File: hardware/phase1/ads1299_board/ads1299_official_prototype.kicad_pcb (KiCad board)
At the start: 4 copper layers, 117 parts, among them J3 Conn_02x10_Odd_Even, J6 36PIN_IDC, U1 ADS1299IPAG, U10 24AA256-I/ST, U4 OPA376

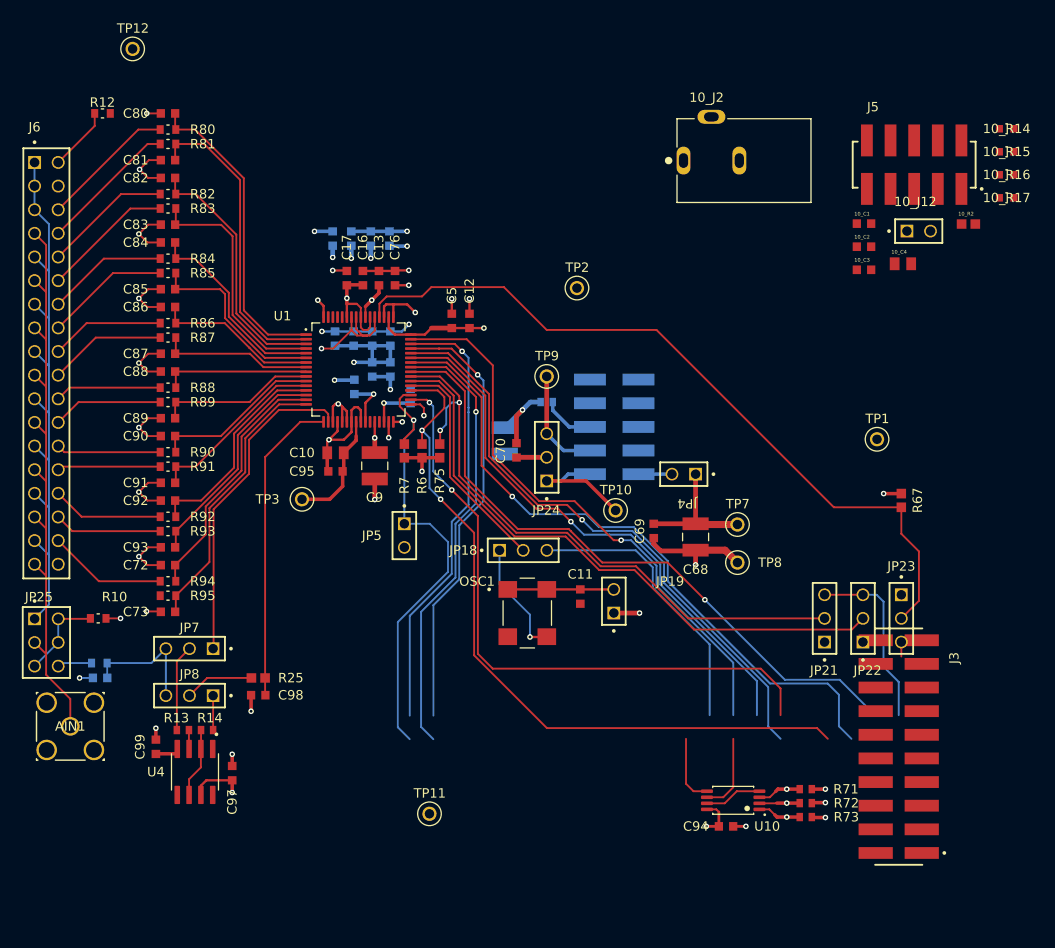
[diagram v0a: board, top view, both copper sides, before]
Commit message: ADS1299 Updated J3 and organized routes, speeding up placement and routing
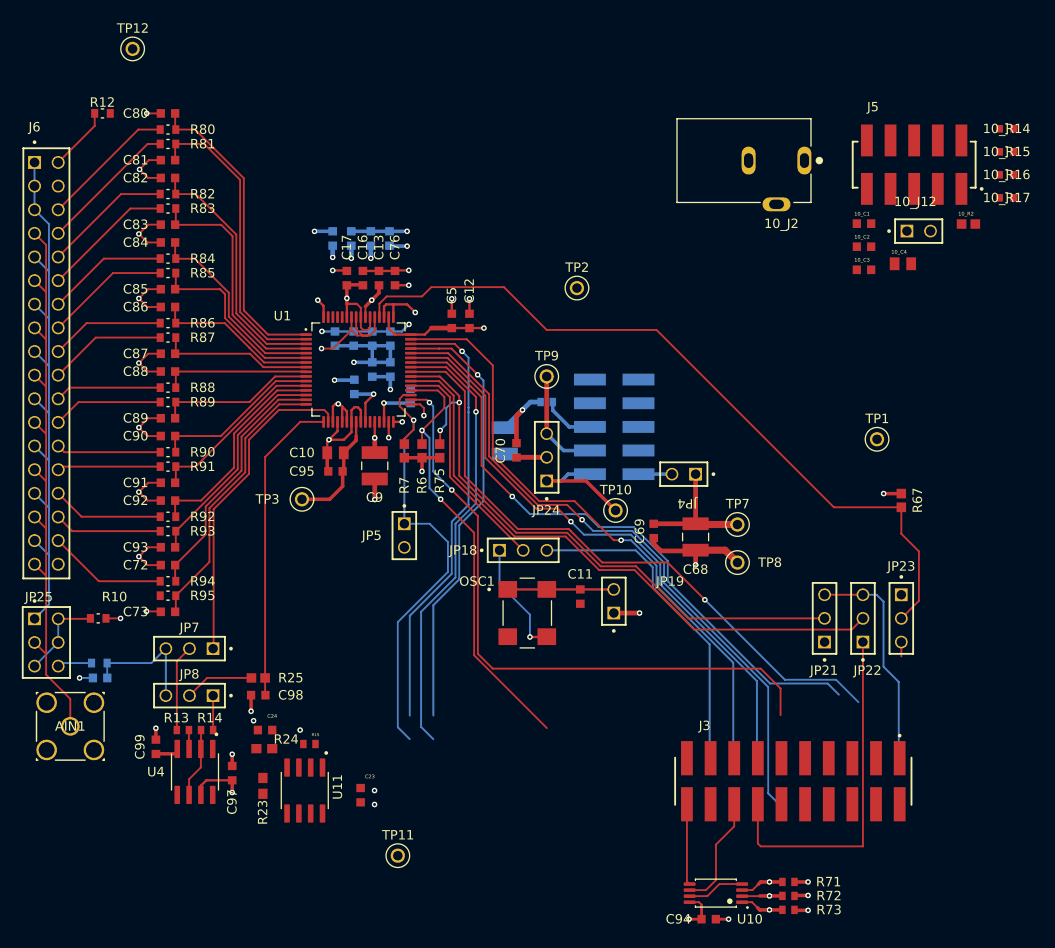
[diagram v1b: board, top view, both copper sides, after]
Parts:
- added C23: CAPC1608X90N, GRM188R61E105KA12D:CAPC1608X90N, F.Cu at (127.0, 97.0)
- added C24: CAPC1608X90N, GRM188R61E105KA12D:CAPC1608X90N, F.Cu at (116.7, 90.0)
- added R15: RESC1005X40, RC0402JR-070RL:RESC1005X40, F.Cu at (121.5, 91.5)
- added R23: 0603, RC0603JR-072ML:0603, F.Cu at (116.5, 96.0)
- added R24: 0603, RC0603JR-072ML:0603, F.Cu at (116.7, 92.0)
- added U11: SOIC127P599X175-8N, OPA376AID:SOIC127P599X175-8N, F.Cu at (121.0, 96.5)
- moved J3 11.9 mm to (173.5, 95.5), turned to 0 degrees
- moved C94 10.1 mm to (164.4, 110.3)
- moved R71 10.1 mm to (173.0, 106.3)
- moved R72 10.1 mm to (173.0, 107.8)
- moved R73 10.1 mm to (173.0, 109.3)
- moved U10 10.1 mm to (165.2, 107.5)
- moved TP11 5.64 mm to (131.0, 103.5)
- turned 10_J2 to 180 degrees
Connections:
- J3 pad 03: (no net) -> CLK
- J3 pad 06: (no net) -> GPIO1
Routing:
- net Net-(J3-Pin_14): track 0.00 -> 37.7 mm
- net /RESET: track 78.2 -> 47.5 mm
- net GPIO2: track 64.6 -> 71.6 mm
- net GPIO1: track 71.7 -> 66.4 mm
- net SPI_DRDY: track 61.6 -> 66.2 mm
- net Net-(J3-Pin_1): track 19.5 -> 24.1 mm
- net EXT_CLK: track 30.6 -> 35.2 mm
- net SPI_OUT: track 60.4 -> 65.0 mm
- net /SCL: track 8.49 -> 12.2 mm
- net SPI_CLK: track 70.5 -> 68.2 mm
- net /SDA: track 7.41 -> 8.70 mm
- net GNDA: vias 26 -> 30

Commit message: Schematic changes, no more power stuff from external board. Layout work, added power stuff, lots to do
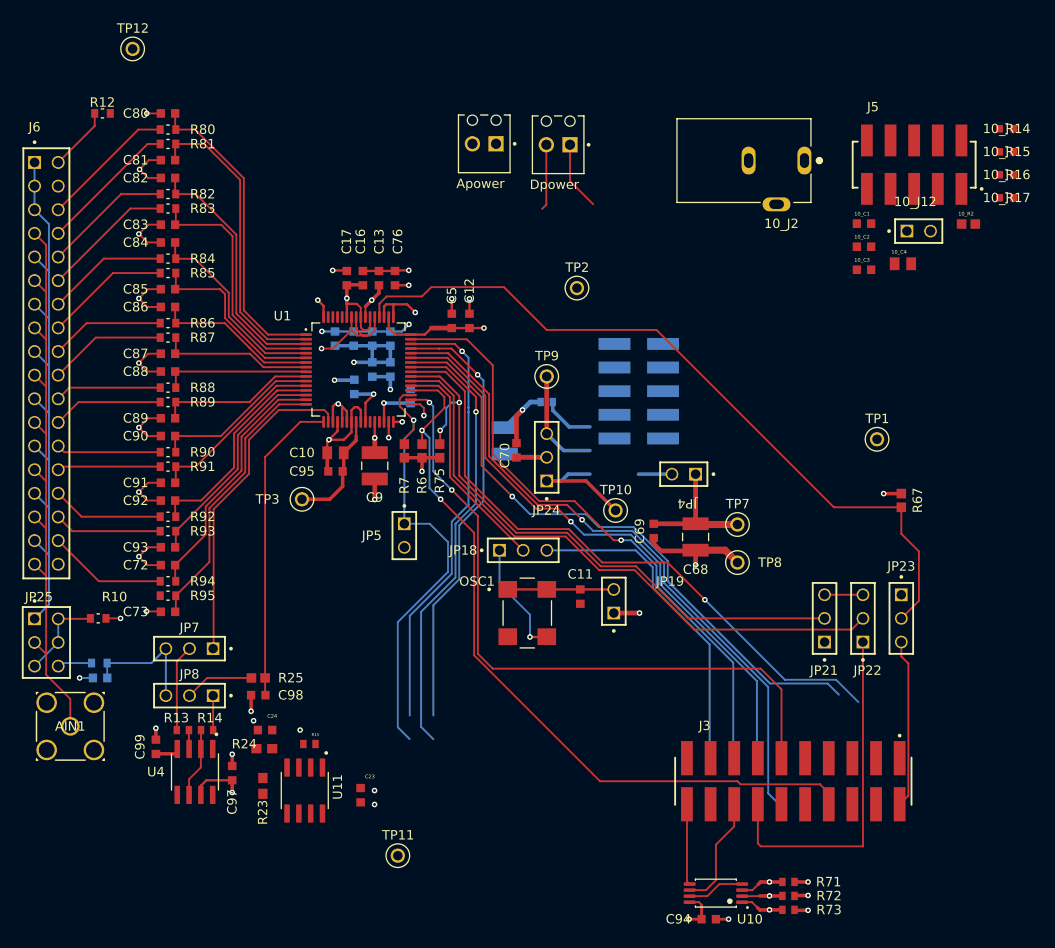
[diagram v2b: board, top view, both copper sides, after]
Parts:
- removed C3, C7, C77, C8: 1uF, GRM188R61E105KA12D:CAPC1608X90N
- added Apower: PHOENIX_1725656, 1725656:PHOENIX_1725656, F.Cu at (143.1, 23.9)
- added Dpower: PHOENIX_1725656, 1725656:PHOENIX_1725656, F.Cu at (151.0, 24.0)
- moved J4 4.66 mm to (156.9, 53.6)
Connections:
- J3 pad 01: (no net) -> GND
- J3 pad 02: (no net) -> Net-(J3-Pin_2)
- J3 pad 04: (no net) -> GNDA
- J3 pad 05: (no net) -> unconnected-(j3-Pin_5-Pad5)
- J3 pad 07: (no net) -> SPI_CS
- J3 pad 08: (no net) -> /RESET
- J3 pad 09: (no net) -> unconnected-(J3-Pin_9-Pad9)
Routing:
- net /RESET: track 47.5 -> 83.0 mm
- net Net-(J3-Pin_1): track 24.1 -> 4.12 mm
- net Net-(J3-Pin_2): track 1.55 -> 18.1 mm
- net GND: track 29.6 -> 37.1 mm
- net DVDD: track 29.9 -> 37.0 mm
- net AVSS: track 52.3 -> 46.3 mm, vias 9 -> 8
- net SPI_IN: track 68.2 -> 72.9 mm
- net GNDA: track 82.5 -> 78.7 mm, vias 30 -> 28
- net AVDD: track 39.6 -> 37.0 mm, vias 6 -> 4
- net VCAP3: track 5.38 -> 4.02 mm, vias 2 -> 1
